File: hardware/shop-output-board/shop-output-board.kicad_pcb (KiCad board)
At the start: 2 copper layers, 150 x 115 mm, 84 parts, among them J1 V+ IN 5-24V, J2 OUT 1-4, J3 OUT 5-8, J4 Pico 1-20, J5 Pico 21-40, Q1 AO3401A, Q2 AO3401A, Q3 AO3401A, Q4 AO3401A, Q5 AO3401A, Q6 AO3401A, Q7 AO3401A, Q8 AO3401A, Q9 AO3401A, U1 PC817B, U2 PC817B, U3 PC817B, U4 PC817B, U5 PC817B, U6 PC817B, U7 PC817B, U8 PC817B

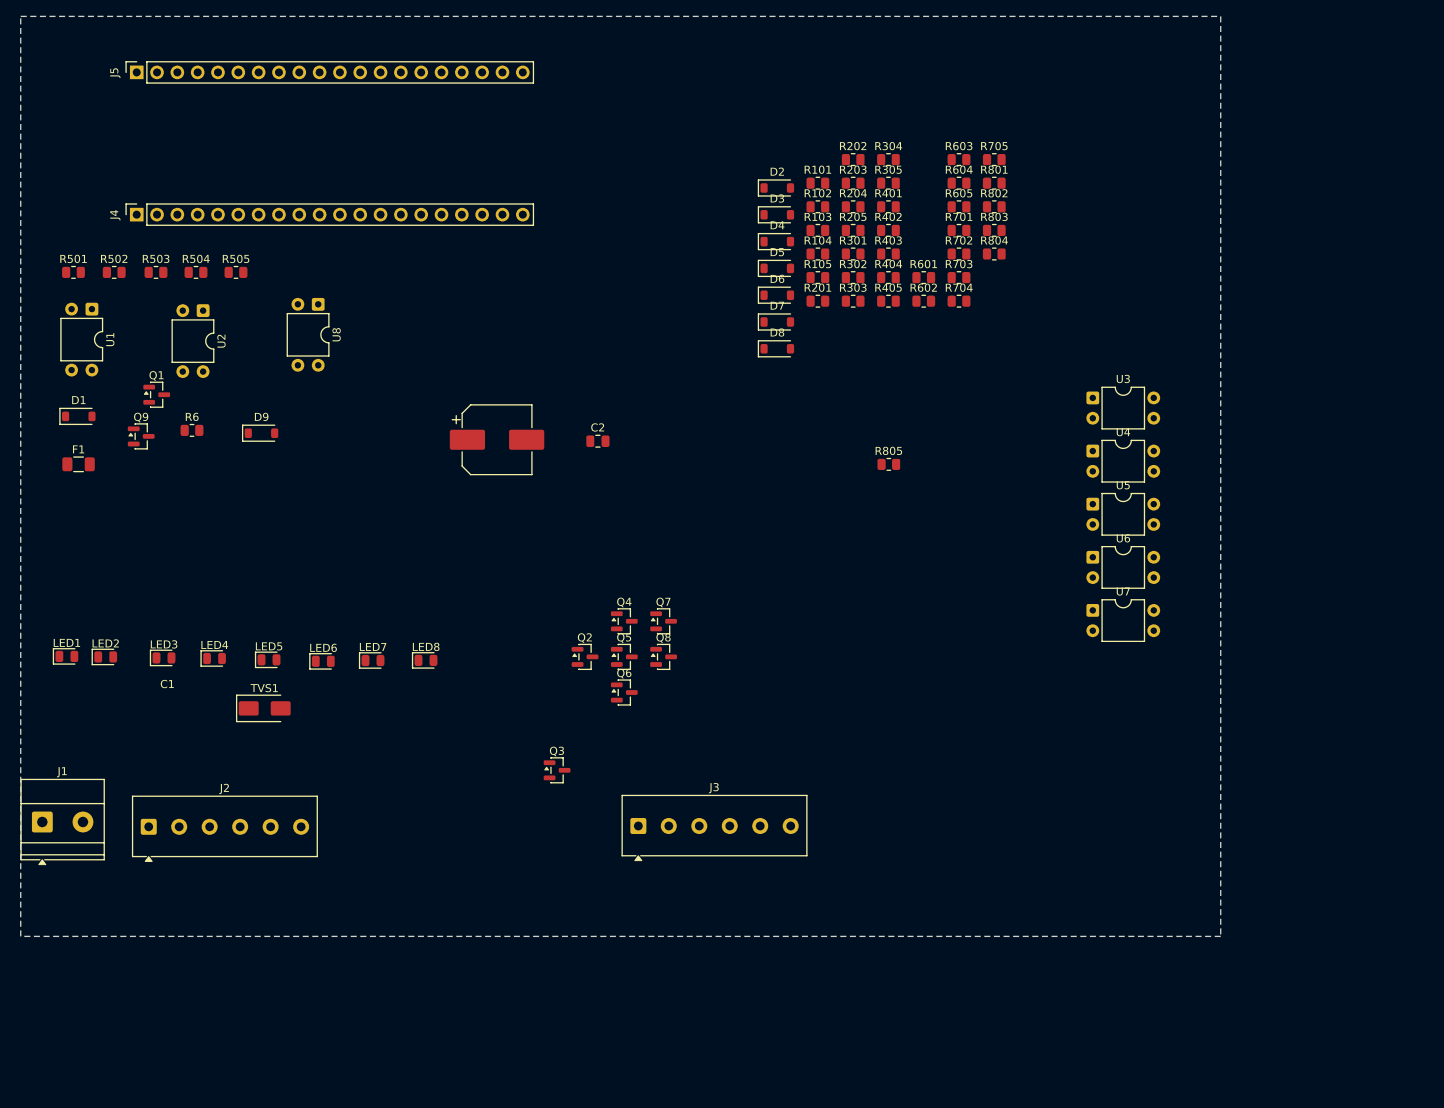
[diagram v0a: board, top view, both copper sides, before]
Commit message: map the input power section, and give it the X positions the plan was missing
The channel diagram covers a block repeated eight times; this section is a
series chain with satellites hanging off it, which reads differently and is
where following the flow gets hard.

layout.md placed the input protection in a y-band but never gave X positions,
which is most of why it was hard to lay out. They are now specified, ordered so
the parts sit in the sequence current actually travels: J1, F1, Q9, then the
shunt trio, ending at the V+ riser.

Three things the drawing makes obvious that the netlist does not:

Q9 is drain-to-input, source-to-output - the opposite way round to the eight
channel MOSFETs, which looks like a mistake right up until you remember why.

R6 and D9 are Q9's gate satellites, not part of the chain, so they go on their
own row beside it rather than in the current path.

TVS1, C1 and C2 are not in series with anything. Each sits from V+ down to the
ground pour, so they are three vias rather than three traces.

The V+ riser is at x=71 because that lands in the gap between channel columns 4
and 5; a riser inside a column would have to fight past R2, D and Q.

Co-Authored-By: Claude Opus 5 <noreply@anthropic.com>
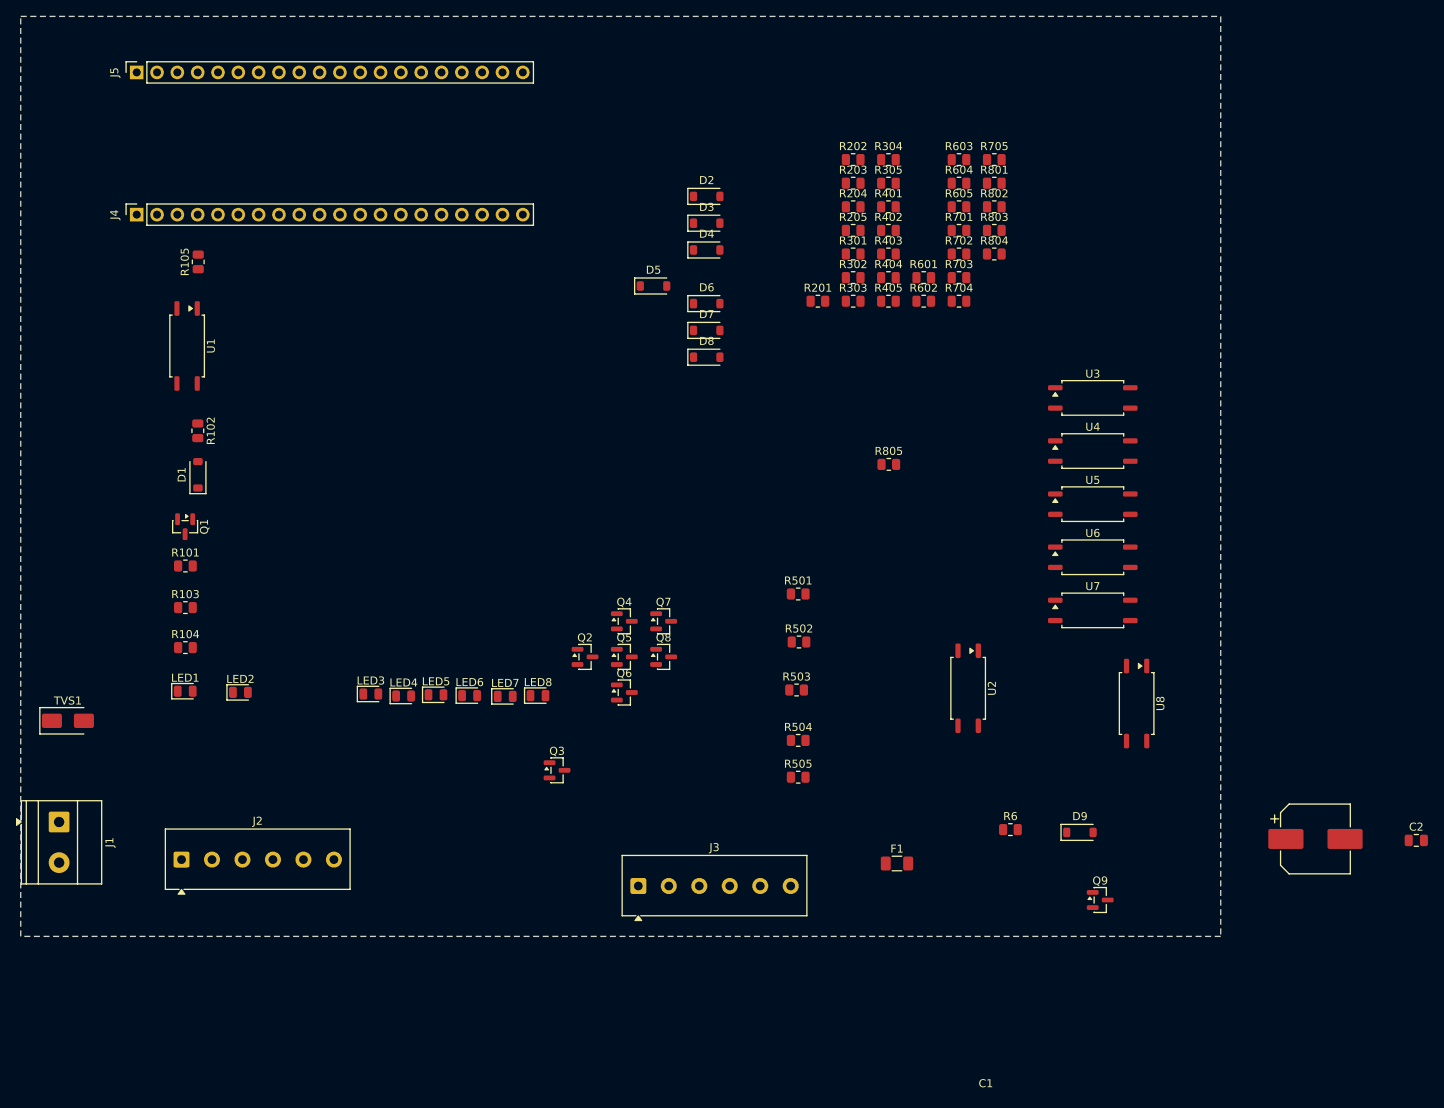
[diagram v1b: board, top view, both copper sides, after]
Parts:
- U1, U2, U3, U4, U5, U6, U7, U8: value PC817B -> LTV-817S (CTR B); footprint Package_DIP:DIP-4_W7.62mm -> Package_SO:SOP-4_7.5x4.1mm_P2.54mm
- moved Q9 133.1 mm to (134.9, 110.5)
- moved D9 113.8 mm to (132.4, 102.0)
- moved R6 113.8 mm to (123.7, 101.7)
- moved U8 113.8 mm to (139.5, 85.9)
- moved F1 113.8 mm to (109.5, 105.9)
- moved C1 113.8 mm to (161.8, 102.8)
- moved C2 113.8 mm to (174.4, 103.0)
- moved U2 106.6 mm to (118.4, 84.0)
- moved R501 99.1 mm to (97.2, 72.2)
- moved R502 97.3 mm to (97.3, 78.2)
- moved R503 95.6 mm to (97.0, 84.2)
- moved R504 95.3 mm to (97.2, 90.5)
- moved R505 94.4 mm to (97.2, 95.1)
- moved R104 93.1 mm to (20.6, 78.9)
- moved R101 92.4 mm to (20.6, 68.7)
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
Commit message: generate the placed board, DRC clean, and fix two rotation bugs it caught
Rather than draw an overlay of suggested traces, this generates a real
.kicad_pcb - because KiCad can check that one. A picture is only as good as my
eyesight; a board file goes through DRC, which knows about clearances,
courtyards and the custom isolation rule.

That paid for itself immediately. Routing against real pad coordinates rather
than assumed ones exposed two placement errors no drawing would have shown:

The SOP-4 optocoupler's 9.38mm isolation span runs along X in the footprint, so
at rotation 0 it straddles a *vertical* barrier. Mine is horizontal. Rotated 90
degrees its pins land at y=35.81 and y=45.19, which is what layout.md claimed
all along - the plan was right and the placement would have been wrong.

The SOT-23 MOSFET puts gate and source on the same side, so the rails had to
swap: V+ left, GATE right, OUT straight down from the drain at bottom-centre.
Rotating it 90 degrees is what makes that work.

DRC also found the R6/D9 row at y=82 overlapping the channel LED row at y=80 -
a clash in my own layout plan. Moved to y=86.

Placement is now 0 violations, 128 unconnected, which is exactly right for an
unrouted board. Route interactively in Pcbnew; the ratsnest is already correct.

Routing is behind --route and is deliberately not the default: it is down from
191 violations to 113 but still has shorts and crossings, and a half-routed
board is worse to inherit than an unrouted one.

Co-Authored-By: Claude Opus 5 <noreply@anthropic.com>
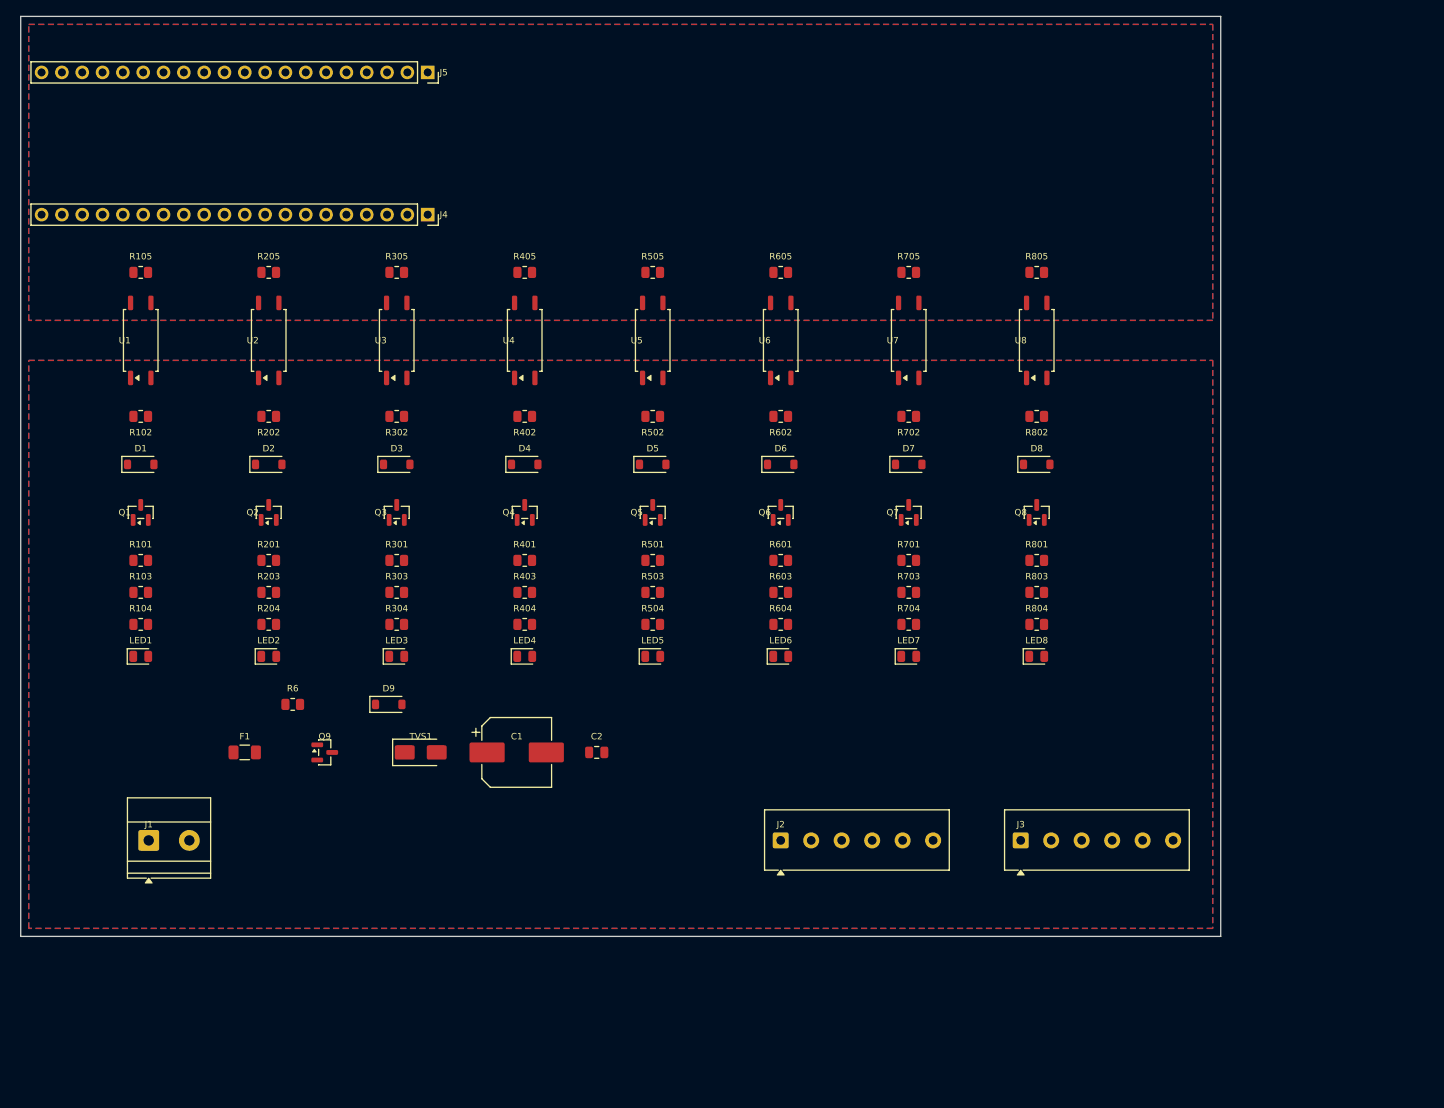
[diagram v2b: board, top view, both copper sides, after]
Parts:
- C1: value 100uF/50V -> (none)
- C2: value 100nF -> (none)
- D1, D2, D3, D4, D5, D6, D7, D8, D9: value MMSZ5237B 8V2 -> (none)
- F1: value 1.1A -> (none)
- J1: value V+ IN 5-24V -> (none)
- J2: value OUT 1-4 -> (none)
- J3: value OUT 5-8 -> (none)
- J4: value Pico 1-20 -> (none)
- J5: value Pico 21-40 -> (none)
- LED1, LED2, LED3, LED4, LED5, LED6, LED7, LED8: value GRN -> (none)
- Q1, Q2, Q3, Q4, Q5, Q6, Q7, Q8, Q9: value AO3401A -> (none)
- R101, R201, R301, R401, R501, R6, R601, R701, R801: value 100k -> (none)
- R102, R202, R302, R402, R502, R602, R702, R802: value 4k7 -> (none)
- R103, R203, R303, R403, R503, R603, R703, R803: value 10k -> (none)
- R104, R204, R304, R404, R504, R604, R704, R804: value 2k2 -> (none)
- R105, R205, R305, R405, R505, R605, R705, R805: value 470R -> (none)
- TVS1: value SMAJ30A -> (none)
- U1, U2, U3, U4, U5, U6, U7, U8: value LTV-817S (CTR B) -> (none)
- moved C2 103.0 mm to (72.0, 92.0)
- moved C1 100.4 mm to (62.0, 92.0)
- moved Q9 98.7 mm to (38.0, 92.0)
- moved U2 97.6 mm to (31.0, 40.5), turned to 90 degrees
- moved R6 91.1 mm to (34.0, 86.0)
- moved R204 89.8 mm to (31.0, 76.0)
- moved R203 89.2 mm to (31.0, 72.0)
- moved D9 87.9 mm to (46.0, 86.0)
- moved U3 87.3 mm to (47.0, 40.5), turned to 90 degrees
- moved R304 84.6 mm to (47.0, 76.0)
- moved F1 82.7 mm to (28.0, 92.0)
- moved R202 79.8 mm to (31.0, 50.0), turned to 180 degrees
- moved R201 75.9 mm to (31.0, 68.0)
- moved J2 74.9 mm to (95.0, 103.0)
- moved R205 73.2 mm to (31.0, 32.0)
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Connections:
- net /GATE1 renamed GATE1
- net /GATE2 renamed GATE2
- net /GATE3 renamed GATE3
- net /GATE4 renamed GATE4
- net /GATE5 renamed GATE5
- net /GATE6 renamed GATE6
- net /GATE7 renamed GATE7
- net /GATE8 renamed GATE8
- net /GP2 renamed GP2
- net /GP3 renamed GP3
- net /GP4 renamed GP4
- net /GP5 renamed GP5
- net /GP6 renamed GP6
- net /GP7 renamed GP7
- net /GP8 renamed GP8
- net /GP9 renamed GP9
- net /ISO_GND renamed ISO_GND
- net /LEDA1 renamed LEDA1
- net /LEDA2 renamed LEDA2
- net /LEDA3 renamed LEDA3
- net /LEDA4 renamed LEDA4
- net /LEDA5 renamed LEDA5
- net /LEDA6 renamed LEDA6
- net /LEDA7 renamed LEDA7
- net /LEDA8 renamed LEDA8
- net /LEDK1 renamed LEDK1
- net /LEDK2 renamed LEDK2
- net /LEDK3 renamed LEDK3
- net /LEDK4 renamed LEDK4
- net /LEDK5 renamed LEDK5
- net /LEDK6 renamed LEDK6
- net /LEDK7 renamed LEDK7
- net /LEDK8 renamed LEDK8
- net /OPTOC1 renamed OPTOC1
- net /OPTOC2 renamed OPTOC2
- net /OPTOC3 renamed OPTOC3
- net /OPTOC4 renamed OPTOC4
- net /OPTOC5 renamed OPTOC5
- net /OPTOC6 renamed OPTOC6
- net /OPTOC7 renamed OPTOC7
- net /OPTOC8 renamed OPTOC8
- net /OUT1 renamed OUT1
- net /OUT2 renamed OUT2
- net /OUT3 renamed OUT3
- net /OUT4 renamed OUT4
- net /OUT5 renamed OUT5
- net /OUT6 renamed OUT6
- net /OUT7 renamed OUT7
- net /OUT8 renamed OUT8
- net /PICO_GND renamed PICO_GND
- net /Q9GATE renamed Q9GATE
- net /V+ renamed V+
- net /VIN_F renamed VIN_F
- net /VIN_RAW renamed VIN_RAW
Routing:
- added copper zone on B.Cu, net ISO_GND
- added copper zone on F.Cu, net ISO_GND
- added copper zone on B.Cu, net PICO_GND
- added copper zone on F.Cu, net PICO_GND

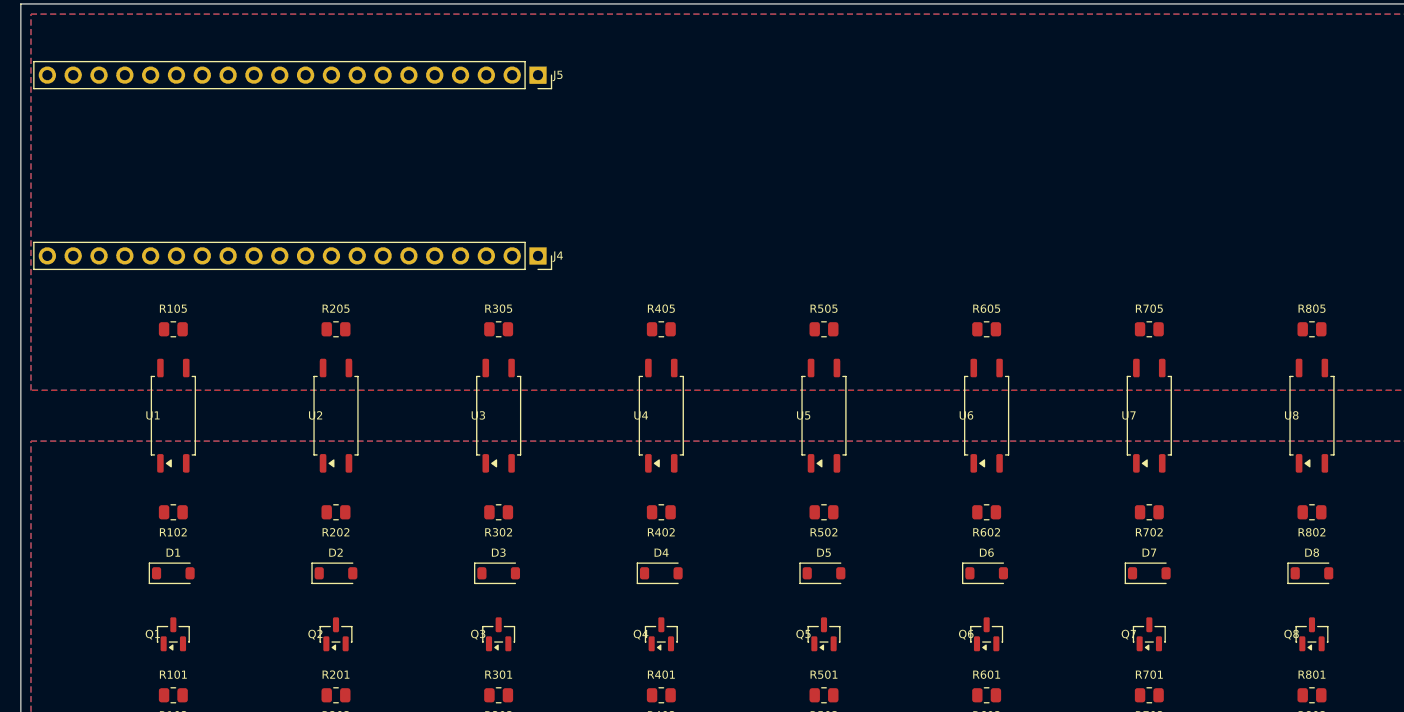
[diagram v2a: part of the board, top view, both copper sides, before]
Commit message: fix inverted pad rotation, and make the GP-to-channel map one setting
Jay spotted the optocouplers were upside down in Pcbnew: pins 3 and 4, the
isolated side, were sitting in the logic zone. The cause was the rotation
transform in generate_pcb.py using the textbook rotation matrix. KiCad rotates
counter-clockwise on screen with Y growing downward, so the signs are not the
textbook ones, and every rotated part landed mirrored.

It looked correct in the generator's own output because the generator was
checking itself against its own bad maths. verify_pcb.py now closes that loop:
it exports IPC-D-356, which carries KiCad's resolved pad coordinates, and
asserts they match - then asserts the thing that actually matters, that no
logic net sits below the barrier and no isolated net above it. 183 pads agree
to 0.05mm.

Optos and MOSFETs move from 90 to 270 degrees as a result; the Pico sockets
from -90 to 90. The J4 sanity check missed this because it only tested which
axis the pads ran along, not which direction.

Separately: the Pico GPIO assigned to each channel is now CHANNEL_GP, imported
by both generators, so reordering it to suit the layout cannot leave the
schematic and the board disagreeing. The firmware drives whatever pin the host
names, so a remap only needs matching pin numbers in the app's GPIO config.

ERC 0, netlist assertions pass, DRC 0 violations.

Co-Authored-By: Claude Opus 5 <noreply@anthropic.com>
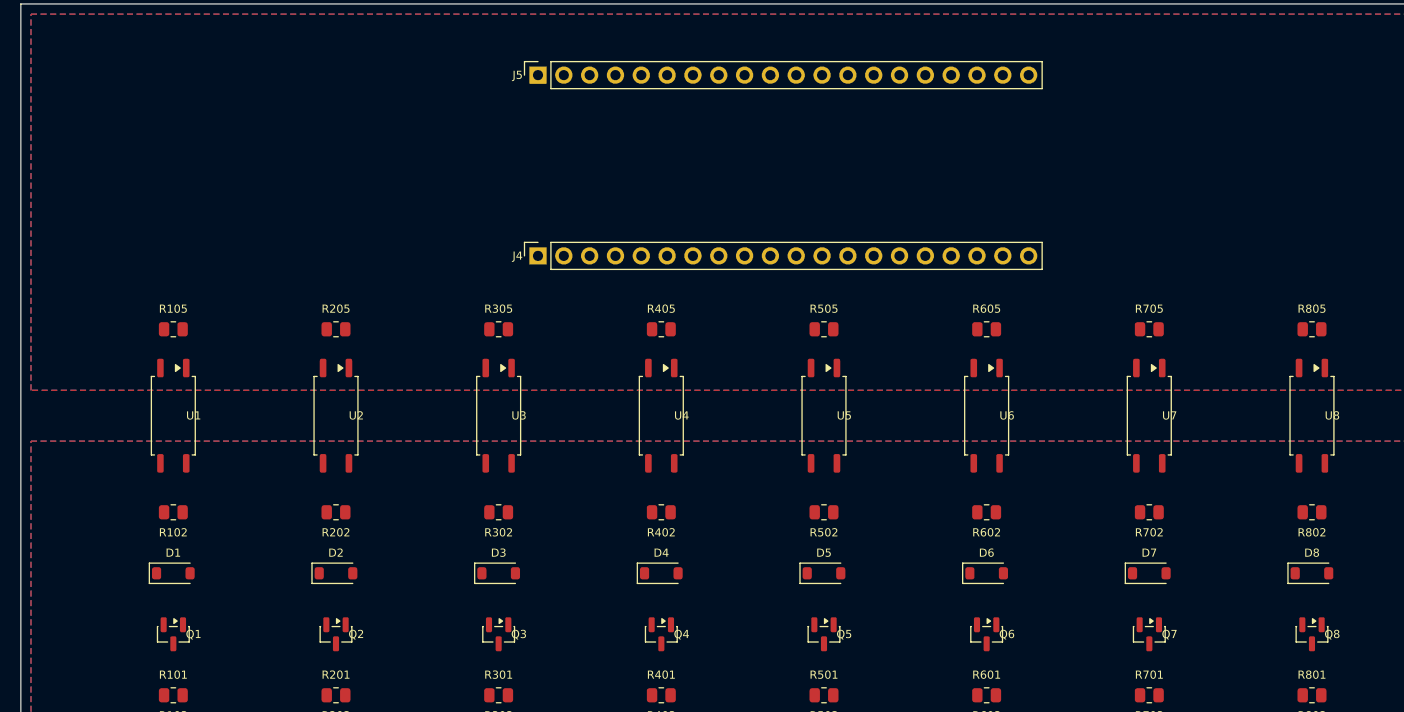
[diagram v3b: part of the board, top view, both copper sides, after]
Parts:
- turned J4 to 90 degrees
- turned J5 to 90 degrees
- turned Q1 to 270 degrees
- turned Q2 to 270 degrees
- turned Q3 to 270 degrees
- turned Q4 to 270 degrees
- turned Q5 to 270 degrees
- turned Q6 to 270 degrees
- turned Q7 to 270 degrees
- turned Q8 to 270 degrees
- turned U1 to 270 degrees
- turned U2 to 270 degrees
- turned U3 to 270 degrees
- turned U4 to 270 degrees
- turned U5 to 270 degrees
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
